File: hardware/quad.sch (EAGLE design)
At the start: 68 parts, among them IC1 BNO055, J501 I2C_TEST, U101 STM32F427VGT6, U202 AND_GATE, U203 SN74AHC1G32DBVR, U401 FT232R, U402 USB-MICROB, U403 LD1117, U404 MFS201N-16-Z, X101 24MHz, Y501 32.768kHz

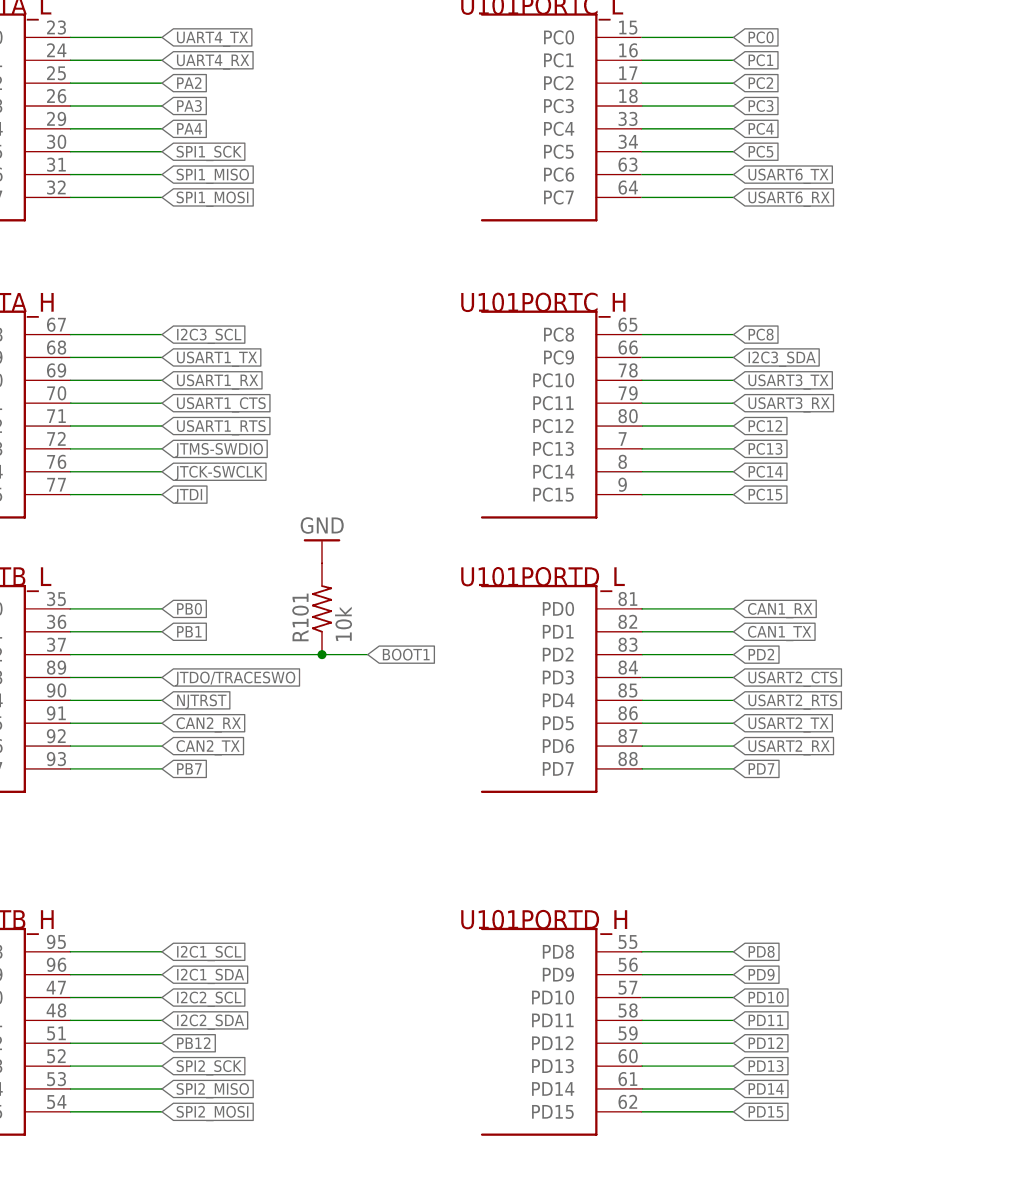
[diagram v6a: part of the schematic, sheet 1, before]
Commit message: Passing DRC on the layout
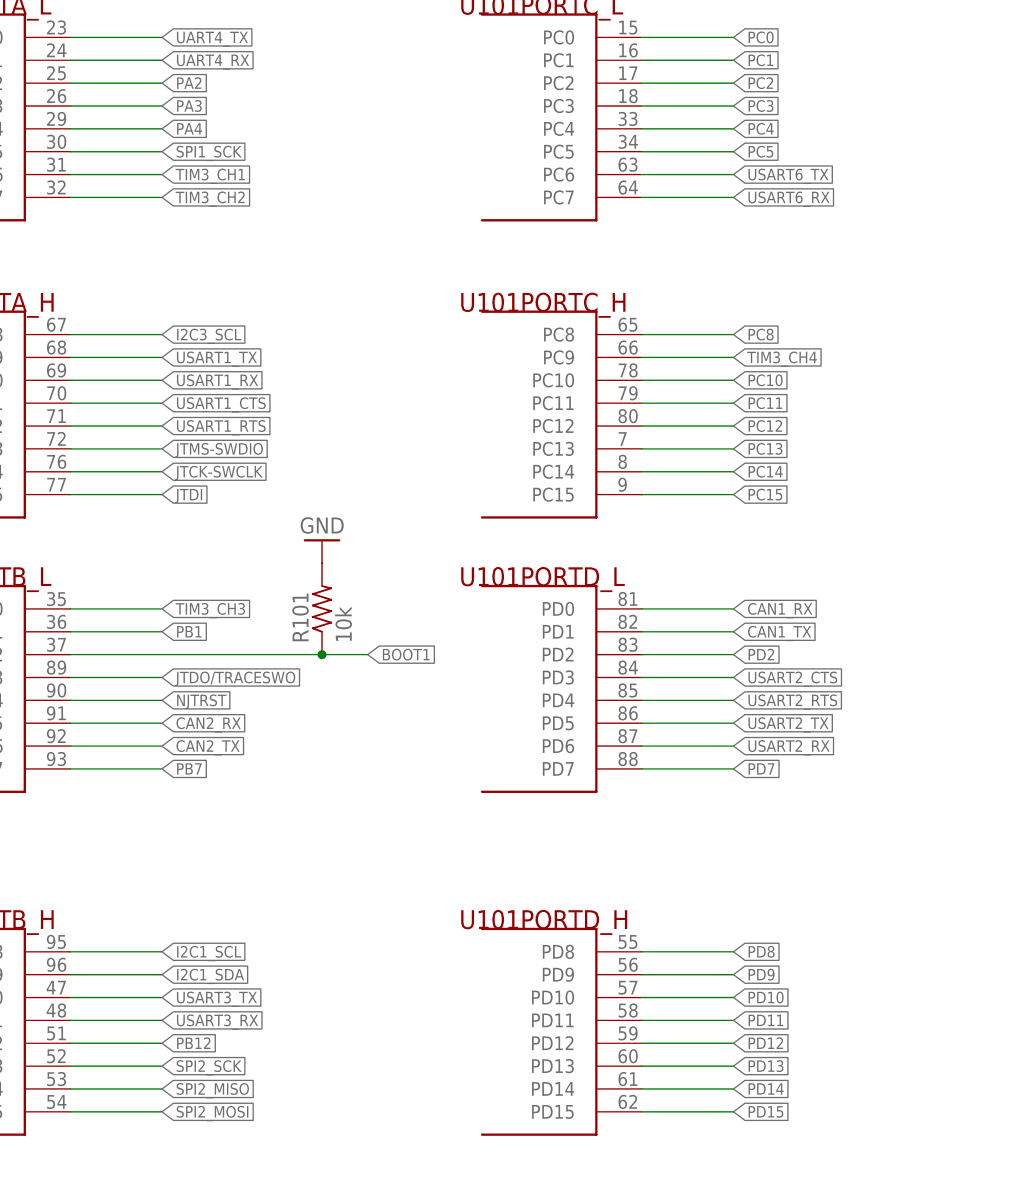
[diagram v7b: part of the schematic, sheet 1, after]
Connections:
- removed net I2C2_SCL: U101PORTB_H.PB10
- removed net I2C2_SDA: U101PORTB_H.PB11
- removed net I2C3_SDA: U101PORTC_H.PC9
- removed net PB0: U101PORTB_L.PB0
- removed net PWM1: ESC1.PWM
- removed net PWM2: ESC2.PWM
- removed net PWM3: ESC3.PWM
- removed net PWM4: ESC4.PWM
- removed net SPI1_MISO: U101PORTA_L.PA6
- removed net SPI1_MOSI: U101PORTA_L.PA7
- new net PC10: U101PORTC_H.PC10
- new net PC11: U101PORTC_H.PC11
- new net TIM3_CH1: ESC2.PWM, U101PORTA_L.PA6
- new net TIM3_CH2: ESC3.PWM, U101PORTA_L.PA7
- new net TIM3_CH3: ESC4.PWM, U101PORTB_L.PB0
- new net TIM3_CH4: ESC1.PWM, U101PORTC_H.PC9
- net USART3_RX: now also U101PORTB_H.PB11; no longer U101PORTC_H.PC11
- net USART3_TX: now also U101PORTB_H.PB10; no longer U101PORTC_H.PC10

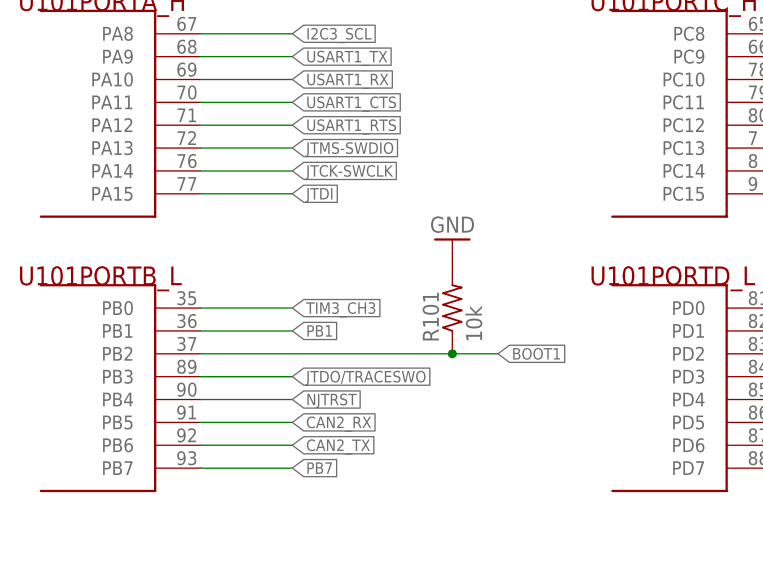
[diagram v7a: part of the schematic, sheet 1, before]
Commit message: Redo board power layout
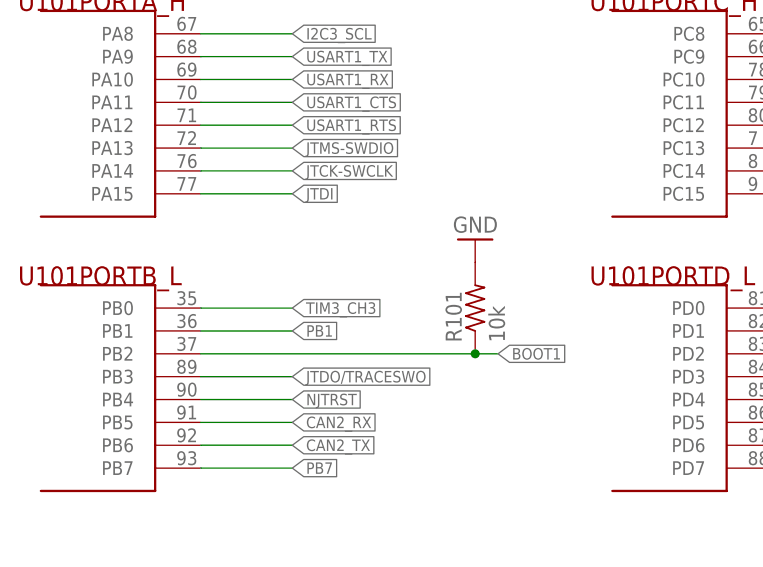
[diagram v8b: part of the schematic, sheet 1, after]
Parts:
- removed BNO_NBOOTLD, BNO_NRST: TESTPAD, quad:TESTPAD
- renumbered U$1 to J701, U$2 to U701
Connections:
- removed net N$13: BNO_NRST.PIN, IC1.11
- net N$16: no longer BNO_NBOOTLD.PIN
- net VBATT: now also U404.1; no longer U404.3
- net VBUS: now also U404.3; no longer U404.1
- net XBEE_DIO4: now also U404.4; no longer U404.6
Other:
- moved on the sheet: R101
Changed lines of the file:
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@@
 <part name="GND43" library="quad" deviceset="GND" device=""/>
 <part name="R501" library="quad" deviceset="R-US_" device="R0603" value="10k"/>
-<part name="BNO_NRST" library="quad" deviceset="TESTPAD" device=""/>
 <part name="R502" library="quad" deviceset="R-US_" device="R0603" value="10k"/>
 <part name="R503" library="quad" deviceset="R-US_" device="R0603" value="10k"/>
@@
 <part name="GND45" library="quad" deviceset="GND" device=""/>
 <part name="R504" library="quad" deviceset="R-US_" device="R0603" value="10k"/>
-<part name="BNO_NBOOTLD" library="quad" deviceset="TESTPAD" device=""/>
 <part name="R505" library="quad" deviceset="R-US_" device="R0603" value="10k"/>
 <part name="R506" library="quad" deviceset="R-US_" device="R0603" value="10k"/>
 <part name="J501" library="quad" deviceset="PINHD-1X2" device="" value="I2C_TEST"/>
-<part name="U$1" library="quad" deviceset="XT60" device=""/>
+<part name="J701" library="quad" deviceset="XT60" device=""/>
 <part name="GND46" library="quad" deviceset="GND" device=""/>
 <part name="GND47" library="quad" deviceset="GND" device=""/>
 <part name="U404" library="quad" deviceset="MFS201N-16-Z" device=""/>
-<part name="U$2" library="quad" deviceset="PSMN9RS-30YLC" device=""/>
+<part name="U701" library="quad" deviceset="PSMN9RS-30YLC" device=""/>
 <part name="R701" library="quad" deviceset="R-US_" device="R0603" value="10k"/>
 <part name="GND48" library="quad" deviceset="GND" device=""/>
@@
 <instance part="GND2" gate="1" x="200.66" y="114.3" rot="R180"/>
 <instance part="GND3" gate="1" x="226.06" y="96.52" rot="R90"/>
-<instance part="GND29" gate="1" x="76.2" y="124.46" rot="R180"/>
-<instance part="R101" gate="G$1" x="76.2" y="116.84" rot="R90"/>
+<instance part="GND29" gate="1" x="78.74" y="124.46" rot="R180"/>
+<instance part="R101" gate="G$1" x="78.74" y="116.84" rot="R90"/>
 </instances>
 <busses>
@@
 <segment>
 <pinref part="U101" gate="PORTB_L" pin="PB2"/>
-<wire x1="48.26" y1="111.76" x2="76.2" y2="111.76" width="0.1524" layer="91"/>
+<wire x1="48.26" y1="111.76" x2="78.74" y2="111.76" width="0.1524" layer="91"/>
 <label x="81.28" y="111.76" size="1.27" layer="95" xref="yes"/>
 <pinref part="R101" gate="G$1" pin="1"/>
-<wire x1="76.2" y1="111.76" x2="81.28" y2="111.76" width="0.1524" layer="91"/>
-<junction x="76.2" y="111.76"/>
+<wire x1="78.74" y1="111.76" x2="81.28" y2="111.76" width="0.1524" layer="91"/>
+<junction x="78.74" y="111.76"/>
 </segment>
 </net>
@@
 </segment>
 <segment>
-<pinref part="U404" gate="G$1" pin="1"/>
-<wire x1="101.6" y1="101.6" x2="91.44" y2="101.6" width="0.1524" layer="91"/>
-<label x="91.44" y="101.6" size="1.778" layer="95" rot="R180" xref="yes"/>
+<pinref part="U404" gate="G$1" pin="3"/>
+<wire x1="101.6" y1="91.44" x2="91.44" y2="91.44" width="0.1524" layer="91"/>
+<label x="91.44" y="91.44" size="1.778" layer="95" rot="R180" xref="yes"/>
 </segment>
 </net>
@@
 <net name="VBATT" class="0">
 <segment>
-<pinref part="U404" gate="G$1" pin="3"/>
-<wire x1="101.6" y1="91.44" x2="91.44" y2="91.44" width="0.1524" layer="91"/>
-<label x="91.44" y="91.44" size="1.778" layer="95" rot="R180" xref="yes"/>
-</segment>
-</net>
-<net name="XBEE_DIO4" class="0">
-<segment>
-<pinref part="U404" gate="G$1" pin="6"/>
-<wire x1="101.6" y1="76.2" x2="91.44" y2="76.2" width="0.1524" layer="91"/>
-<label x="91.44" y="76.2" size="1.778" layer="95" rot="R180" xref="yes"/>
+<pinref part="U404" gate="G$1" pin="1"/>
+<wire x1="101.6" y1="101.6" x2="91.44" y2="101.6" width="0.1524" layer="91"/>
+<label x="91.44" y="101.6" size="1.778" layer="95" rot="R180" xref="yes"/>
 </segment>
 </net>
@@
 <pinref part="U404" gate="G$1" pin="2"/>
 <wire x1="177.8" y1="96.52" x2="134.62" y2="96.52" width="0.1524" layer="91"/>
+</segment>
+</net>
+<net name="XBEE_DIO4" class="0">
+<segment>
+<pinref part="U404" gate="G$1" pin="4"/>
+<wire x1="101.6" y1="86.36" x2="91.44" y2="86.36" width="0.1524" layer="91"/>
+<label x="91.44" y="86.36" size="1.778" layer="95" rot="R180" xref="yes"/>
 </segment>
 </net>
@@
 <instance part="GND43" gate="1" x="139.7" y="109.22"/>
 <instance part="R501" gate="G$1" x="139.7" y="116.84" rot="R270"/>
-<instance part="BNO_NRST" gate="G$1" x="129.54" y="111.76" rot="R90"/>
 <instance part="R502" gate="G$1" x="149.86" y="99.06"/>
 <instance part="R503" gate="G$1" x="149.86" y="106.68"/>
@@
 <instance part="GND45" gate="1" x="160.02" y="106.68" rot="R90"/>
 <instance part="R504" gate="G$1" x="132.08" y="83.82" rot="R270"/>
-<instance part="BNO_NBOOTLD" gate="G$1" x="137.16" y="93.98" rot="R90"/>
 <instance part="R505" gate="G$1" x="134.62" y="137.16" rot="R270"/>
 <instance part="R506" gate="G$1" x="144.78" y="137.16" rot="R270"/>
@@
 </segment>
 </net>
-<net name="N$13" class="0">
-<segment>
-<pinref part="IC1" gate="G$1" pin="11"/>
-<pinref part="BNO_NRST" gate="G$1" pin="PIN"/>
-<wire x1="124.46" y1="111.76" x2="121.92" y2="111.76" width="0.1524" layer="91"/>
-</segment>
-</net>
 <net name="N$14" class="0">
 <segment>
@@
 <wire x1="121.92" y1="96.52" x2="132.08" y2="96.52" width="0.1524" layer="91"/>
 <wire x1="132.08" y1="96.52" x2="132.08" y2="88.9" width="0.1524" layer="91"/>
-<pinref part="BNO_NBOOTLD" gate="G$1" pin="PIN"/>
 <junction x="132.08" y="88.9"/>
 <wire x1="132.08" y1="88.9" x2="132.08" y2="93.98" width="0.1524" layer="91"/>
@@
 <instance part="FRAME7" gate="G$1" x="0" y="0"/>
 <instance part="FRAME7" gate="G$2" x="172.72" y="0"/>
-<instance part="U$1" gate="G$1" x="63.5" y="109.22"/>
+<instance part="J701" gate="G$1" x="63.5" y="109.22"/>
 <instance part="GND46" gate="1" x="76.2" y="101.6"/>
 <instance part="GND47" gate="1" x="190.5" y="66.04"/>
-<instance part="U$2" gate="G$1" x="190.5" y="83.82"/>
+<instance part="U701" gate="G$1" x="190.5" y="83.82"/>
 <instance part="R701" gate="G$1" x="172.72" y="78.74" rot="R90"/>
 <instance part="GND48" gate="1" x="172.72" y="71.12"/>
@@
 <net name="VBATT" class="0">
 <segment>
-<pinref part="U$1" gate="G$1" pin="PWR"/>
+<pinref part="J701" gate="G$1" pin="PWR"/>
 <wire x1="93.726" y1="111.76" x2="73.66" y2="111.76" width="0.1524" layer="91"/>
 <label x="93.98" y="111.76" size="1.778" layer="95" xref="yes"/>
@@
 <net name="GND" class="0">
 <segment>
-<pinref part="U$1" gate="G$1" pin="GND"/>
+<pinref part="J701" gate="G$1" pin="GND"/>
 <pinref part="GND46" gate="1" pin="GND"/>
 <wire x1="73.66" y1="106.68" x2="76.2" y2="106.68" width="0.1524" layer="91"/>
@@
 <segment>
 <pinref part="GND47" gate="1" pin="GND"/>
-<pinref part="U$2" gate="G$1" pin="S"/>
+<pinref part="U701" gate="G$1" pin="S"/>
 <wire x1="190.5" y1="68.58" x2="190.5" y2="73.66" width="0.1524" layer="91"/>
 </segment>
@@
 <net name="POWER_EN" class="0">
 <segment>
-<pinref part="U$2" gate="G$1" pin="G"/>
+<pinref part="U701" gate="G$1" pin="G"/>
 <wire x1="177.8" y1="83.82" x2="172.72" y2="83.82" width="0.1524" layer="91"/>
 <label x="144.78" y="83.82" size="1.778" layer="95" rot="R180" xref="yes"/>
@@
 <net name="KILL_GND" class="0">
 <segment>
-<pinref part="U$2" gate="G$1" pin="D"/>
+<pinref part="U701" gate="G$1" pin="D"/>
 <wire x1="190.5" y1="93.98" x2="190.5" y2="101.6" width="0.1524" layer="91"/>
 <label x="190.5" y="101.6" size="1.778" layer="95" rot="R90" xref="yes"/>
